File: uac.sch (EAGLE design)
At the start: 206 parts, among them Q6 2N7002CK4SST, Q7 2N7002CK4SST, U2 ADXL345, Y1 RESONATORSMD

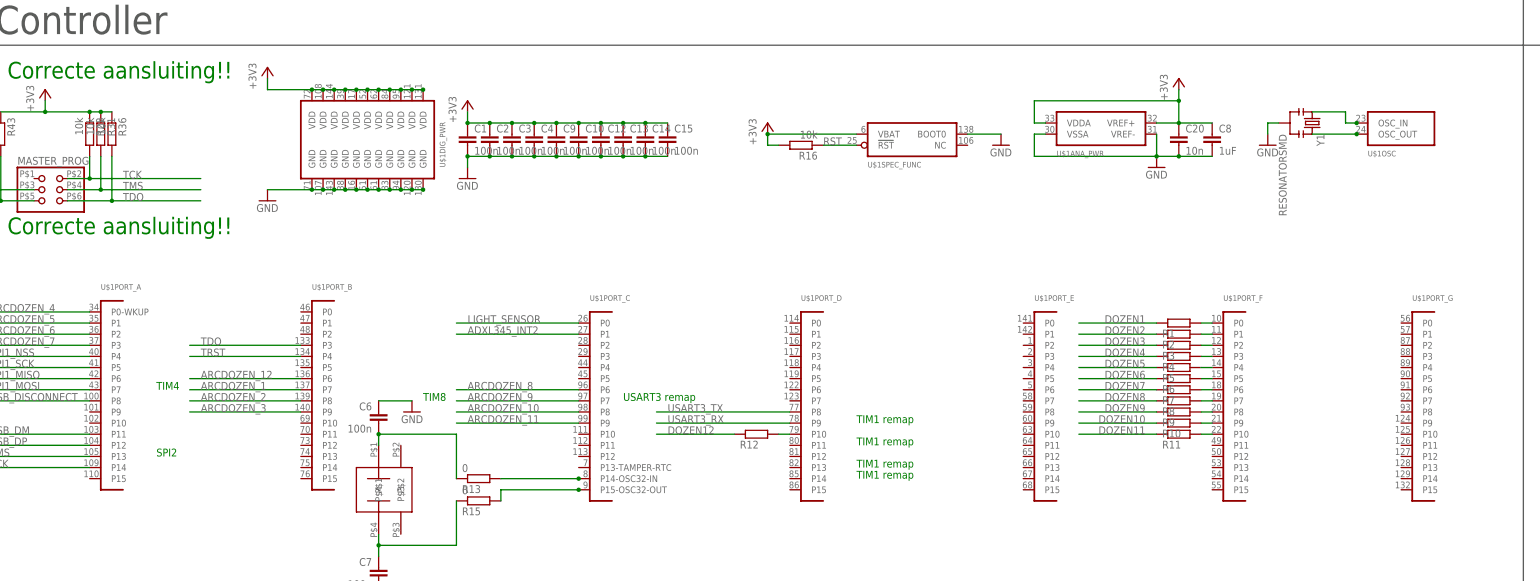
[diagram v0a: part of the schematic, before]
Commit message: Moved to 2 layer
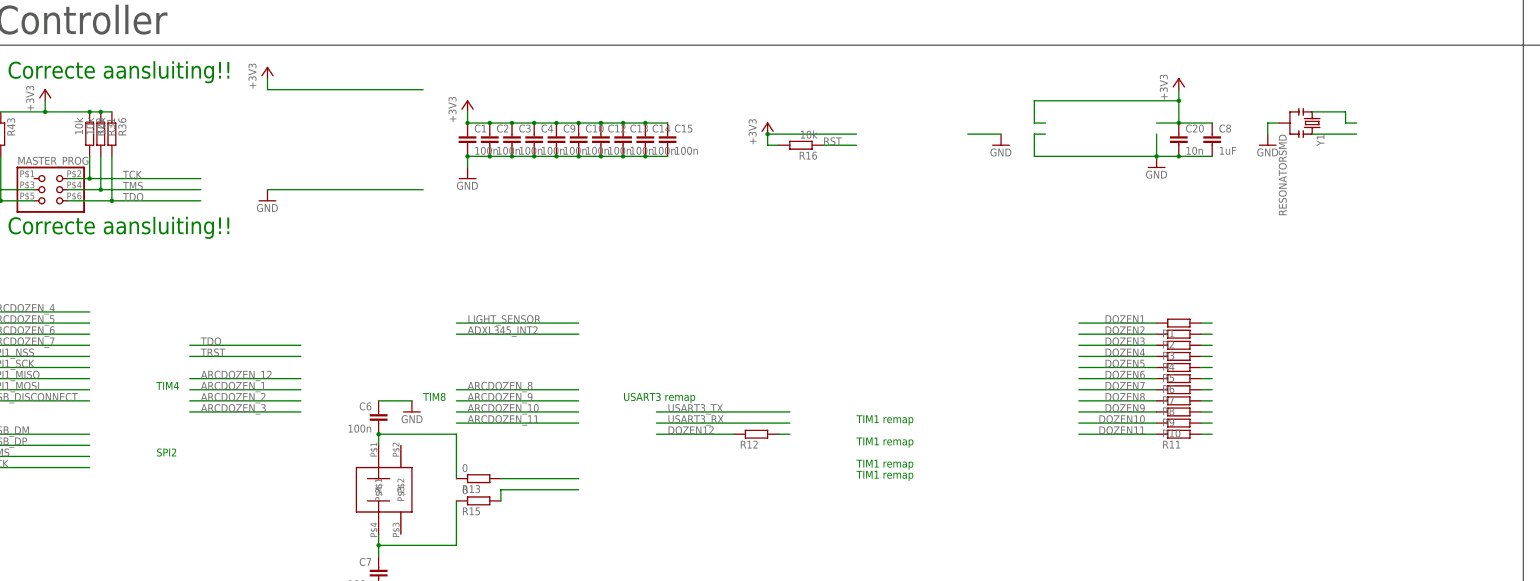
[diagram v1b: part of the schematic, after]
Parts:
- removed U$1: (no value), stm32_lqfp144:STM32F103ZE
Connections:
- net +3V3: no longer U$1ANA_PWR.VDDA, U$1ANA_PWR.VREF+, U$1DIG_PWR.VDD@1, U$1DIG_PWR.VDD@10, U$1DIG_PWR.VDD@11, U$1DIG_PWR.VDD@2, U$1DIG_PWR.VDD@3, U$1DIG_PWR.VDD@4, U$1DIG_PWR.VDD@5, U$1DIG_PWR.VDD@6, U$1DIG_PWR.VDD@7, U$1DIG_PWR.VDD@8, U$1DIG_PWR.VDD@9, U$1SPEC_FUNC.VBAT
- net ADXL345_INT2: no longer U$1PORT_C.P1
- net ARCDOZEN_1: no longer U$1PORT_B.P7
- net ARCDOZEN_10: no longer U$1PORT_C.P8
- net ARCDOZEN_11: no longer U$1PORT_C.P9
- net ARCDOZEN_12: no longer U$1PORT_B.P6
- net ARCDOZEN_2: no longer U$1PORT_B.P8
- net ARCDOZEN_3: no longer U$1PORT_B.P9
- net ARCDOZEN_4: no longer U$1PORT_A.P0-WKUP
- net ARCDOZEN_5: no longer U$1PORT_A.P1
- net ARCDOZEN_6: no longer U$1PORT_A.P2
- net ARCDOZEN_7: no longer U$1PORT_A.P3
- net ARCDOZEN_8: no longer U$1PORT_C.P6
- net ARCDOZEN_9: no longer U$1PORT_C.P7
- net GND: no longer U$1ANA_PWR.VREF-, U$1ANA_PWR.VSSA, U$1DIG_PWR.GND@1, U$1DIG_PWR.GND@10, U$1DIG_PWR.GND@11, U$1DIG_PWR.GND@2, U$1DIG_PWR.GND@3, U$1DIG_PWR.GND@4, U$1DIG_PWR.GND@5, U$1DIG_PWR.GND@6, U$1DIG_PWR.GND@7, U$1DIG_PWR.GND@8, U$1DIG_PWR.GND@9, U$1SPEC_FUNC.BOOT0
- net LIGHT_SENSOR: no longer U$1PORT_C.P0
- net N$1: no longer U$1OSC.OSC_OUT
- net N$10: no longer U$1PORT_F.P3
- net N$11: no longer U$1PORT_F.P4
- net N$12: no longer U$1PORT_F.P5
- net N$13: no longer U$1PORT_F.P6
- net N$14: no longer U$1PORT_F.P7
- net N$15: no longer U$1PORT_F.P8
- net N$16: no longer U$1PORT_F.P9
- net N$17: no longer U$1PORT_F.P10
- net N$2: no longer U$1OSC.OSC_IN
- net N$3: no longer U$1PORT_C.P15-OSC32-OUT
- net N$35: no longer U$1PORT_D.P10
- net N$4: no longer U$1PORT_C.P14-OSC32-IN
- net N$7: no longer U$1PORT_F.P0
- net N$8: no longer U$1PORT_F.P1
- net N$9: no longer U$1PORT_F.P2
- net RST: no longer U$1SPEC_FUNC.!RST
- net SPI1_MISO: no longer U$1PORT_A.P6
- net SPI1_MOSI: no longer U$1PORT_A.P7
- net SPI1_NSS: no longer U$1PORT_A.P4
- net SPI1_SCK: no longer U$1PORT_A.P5
- net TCK: no longer U$1PORT_A.P14
- net TDO: no longer U$1PORT_B.P3
- net TMS: no longer U$1PORT_A.P13
- net TRST: no longer U$1PORT_B.P4
- net USART3_RX: no longer U$1PORT_D.P9
- net USART3_TX: no longer U$1PORT_D.P8
- net USB_DISCONNECT: no longer U$1PORT_A.P8
- net USB_DM: no longer U$1PORT_A.P11
- net USB_DP: no longer U$1PORT_A.P12

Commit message: 64 pin  microcontroller
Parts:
- added U$1: STM32F103CBT6, stm32:STM32F103CBT6
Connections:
- net +3V3: now also U$1.VBAT, U$1.VDD_1, U$1.VDD_2, U$1.VDD_3, U$1.VDD_4, U$1.VDD_A
- net GND: now also U$1.VSS_1, U$1.VSS_2, U$1.VSS_3, U$1.VSS_4, U$1.VSS_A
- net N$3: now also U$1.PC14-OSC32_IN
- net N$4: now also U$1.PC15-OSC32_OUT
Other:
- moved on the sheet: C6, C7, R13, R15
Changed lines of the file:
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@@
 <part name="GND9" library="Custom components" deviceset="GND" device=""/>
 <part name="+3V7" library="supply1" deviceset="+3V3" device=""/>
-<part name="GND10" library="Custom components" deviceset="GND" device=""/>
 <part name="R16" library="Custom components" deviceset="R-EU_" device="R0603" value="10k"/>
 <part name="C9" library="Custom components" deviceset="C-EU" device="C0603" value="100n"/>
@@
 <part name="P+3" library="Custom components" deviceset="+5V" device=""/>
 <part name="JP1" library="SparkFun2012" deviceset="JUMPER-2" device="SMD-NO"/>
+<part name="U$1" library="stm32" deviceset="STM32F103CBT6" device=""/>
 </parts>
 <sheets>
@@
 <instance part="R43" gate="G$1" x="25.4" y="215.9" rot="R270"/>
 <instance part="+3V3" gate="G$1" x="35.56" y="226.06"/>
-<instance part="U$2" gate="G$1" x="114.3" y="137.16" rot="MR270"/>
-<instance part="C6" gate="G$1" x="111.76" y="152.4" rot="MR0"/>
-<instance part="C7" gate="G$1" x="111.76" y="116.84" rot="MR0"/>
-<instance part="GND6" gate="1" x="111.76" y="106.68" rot="MR0"/>
-<instance part="GND7" gate="1" x="119.38" y="152.4" rot="MR0"/>
-<instance part="R13" gate="G$1" x="134.62" y="137.16" rot="MR180"/>
-<instance part="R15" gate="G$1" x="134.62" y="132.08" rot="MR180"/>
+<instance part="U$2" gate="G$1" x="231.14" y="342.9" rot="R270"/>
+<instance part="C6" gate="G$1" x="233.68" y="358.14"/>
+<instance part="C7" gate="G$1" x="233.68" y="322.58"/>
+<instance part="GND6" gate="1" x="233.68" y="312.42"/>
+<instance part="GND7" gate="1" x="226.06" y="358.14"/>
+<instance part="R13" gate="G$1" x="210.82" y="342.9" rot="R180"/>
+<instance part="R15" gate="G$1" x="210.82" y="337.82" rot="R180"/>
 <instance part="+3V4" gate="G$1" x="294.64" y="228.6"/>
 <instance part="C20" gate="G$1" x="294.64" y="215.9"/>
 <instance part="C8" gate="G$1" x="302.26" y="215.9"/>
 <instance part="GND8" gate="1" x="289.56" y="208.28"/>
-<instance part="+3V5" gate="G$1" x="86.36" y="231.14"/>
-<instance part="GND9" gate="1" x="86.36" y="200.66"/>
+<instance part="+3V5" gate="G$1" x="154.94" y="401.32"/>
+<instance part="GND9" gate="1" x="154.94" y="299.72"/>
 <instance part="+3V7" gate="G$1" x="200.66" y="218.44"/>
-<instance part="GND10" gate="1" x="254" y="213.36"/>
 <instance part="R16" gate="G$1" x="208.28" y="213.36" rot="R180"/>
 <instance part="C9" gate="G$1" x="152.4" y="215.9"/>
@@
 <instance part="P+3" gate="1" x="424.18" y="134.62"/>
 <instance part="JP1" gate="A" x="419.1" y="134.62"/>
+<instance part="U$1" gate="G$1" x="149.86" y="363.22"/>
 </instances>
 <busses>
@@
 <pinref part="C7" gate="G$1" pin="2"/>
 <pinref part="GND6" gate="1" pin="GND"/>
-<wire x1="111.76" y1="109.22" x2="111.76" y2="111.76" width="0.1524" layer="91"/>
+<wire x1="233.68" y1="314.96" x2="233.68" y2="317.5" width="0.1524" layer="91"/>
 </segment>
 <segment>
 <pinref part="C6" gate="G$1" pin="1"/>
 <pinref part="GND7" gate="1" pin="GND"/>
-<wire x1="111.76" y1="154.94" x2="119.38" y2="154.94" width="0.1524" layer="91"/>
+<wire x1="233.68" y1="360.68" x2="226.06" y2="360.68" width="0.1524" layer="91"/>
 </segment>
 <segment>
@@
 <pinref part="GND8" gate="1" pin="GND"/>
 <wire x1="294.64" y1="210.82" x2="289.56" y2="210.82" width="0.1524" layer="91"/>
-<wire x1="289.56" y1="210.82" x2="289.56" y2="215.9" width="0.1524" layer="91"/>
-<wire x1="264.16" y1="215.9" x2="261.62" y2="215.9" width="0.1524" layer="91"/>
-<wire x1="261.62" y1="215.9" x2="261.62" y2="210.82" width="0.1524" layer="91"/>
-<wire x1="261.62" y1="210.82" x2="289.56" y2="210.82" width="0.1524" layer="91"/>
-<junction x="289.56" y="210.82"/>
 <junction x="294.64" y="210.82"/>
-</segment>
-<segment>
-<wire x1="121.92" y1="203.2" x2="86.36" y2="203.2" width="0.1524" layer="91"/>
-<pinref part="GND9" gate="1" pin="GND"/>
-</segment>
-<segment>
-<pinref part="GND10" gate="1" pin="GND"/>
-<wire x1="246.38" y1="215.9" x2="254" y2="215.9" width="0.1524" layer="91"/>
 </segment>
 <segment>
@@
 <wire x1="175.26" y1="20.32" x2="177.8" y2="20.32" width="0.1524" layer="91"/>
 </segment>
+<segment>
+<pinref part="GND9" gate="1" pin="GND"/>
+<pinref part="U$1" gate="G$1" pin="VSS_A"/>
+<wire x1="154.94" y1="302.26" x2="154.94" y2="304.8" width="0.1524" layer="91"/>
+<pinref part="U$1" gate="G$1" pin="VSS_1"/>
+<wire x1="154.94" y1="304.8" x2="160.02" y2="304.8" width="0.1524" layer="91"/>
+<pinref part="U$1" gate="G$1" pin="VSS_2"/>
+<wire x1="160.02" y1="304.8" x2="162.56" y2="304.8" width="0.1524" layer="91"/>
+<pinref part="U$1" gate="G$1" pin="VSS_3"/>
+<wire x1="162.56" y1="304.8" x2="165.1" y2="304.8" width="0.1524" layer="91"/>
+<pinref part="U$1" gate="G$1" pin="VSS_4"/>
+<wire x1="165.1" y1="304.8" x2="167.64" y2="304.8" width="0.1524" layer="91"/>
+<junction x="154.94" y="304.8"/>
+<junction x="160.02" y="304.8"/>
+<junction x="162.56" y="304.8"/>
+<junction x="165.1" y="304.8"/>
+<junction x="167.64" y="304.8"/>
+</segment>
 </net>
 <net name="+3V3" class="0">
@@
 </segment>
 <segment>
-<wire x1="289.56" y1="218.44" x2="294.64" y2="218.44" width="0.1524" layer="91"/>
-<wire x1="294.64" y1="218.44" x2="294.64" y2="223.52" width="0.1524" layer="91"/>
-<wire x1="294.64" y1="223.52" x2="261.62" y2="223.52" width="0.1524" layer="91"/>
-<wire x1="261.62" y1="223.52" x2="261.62" y2="218.44" width="0.1524" layer="91"/>
-<wire x1="261.62" y1="218.44" x2="264.16" y2="218.44" width="0.1524" layer="91"/>
+<wire x1="294.64" y1="218.44" x2="294.64" y2="226.06" width="0.1524" layer="91"/>
 <pinref part="+3V4" gate="G$1" pin="+3V3"/>
-<wire x1="294.64" y1="226.06" x2="294.64" y2="223.52" width="0.1524" layer="91"/>
-<junction x="294.64" y="223.52"/>
 <pinref part="C20" gate="G$1" pin="1"/>
 <pinref part="C8" gate="G$1" pin="1"/>
 <wire x1="294.64" y1="218.44" x2="302.26" y2="218.44" width="0.1524" layer="91"/>
 <junction x="294.64" y="218.44"/>
-</segment>
-<segment>
-<wire x1="121.92" y1="226.06" x2="86.36" y2="226.06" width="0.1524" layer="91"/>
-<pinref part="+3V5" gate="G$1" pin="+3V3"/>
-<wire x1="86.36" y1="228.6" x2="86.36" y2="226.06" width="0.1524" layer="91"/>
 </segment>
 <segment>
@@
 <wire x1="177.8" y1="7.62" x2="177.8" y2="10.16" width="0.1524" layer="91"/>
 </segment>
+<segment>
+<pinref part="U$1" gate="G$1" pin="VBAT"/>
+<pinref part="U$1" gate="G$1" pin="VDD_4"/>
+<wire x1="172.72" y1="391.16" x2="167.64" y2="391.16" width="0.1524" layer="91"/>
+<pinref part="U$1" gate="G$1" pin="VDD_3"/>
+<wire x1="167.64" y1="391.16" x2="165.1" y2="391.16" width="0.1524" layer="91"/>
+<pinref part="U$1" gate="G$1" pin="VDD_2"/>
+<wire x1="165.1" y1="391.16" x2="162.56" y2="391.16" width="0.1524" layer="91"/>
+<pinref part="U$1" gate="G$1" pin="VDD_1"/>
+<wire x1="162.56" y1="391.16" x2="160.02" y2="391.16" width="0.1524" layer="91"/>
+<pinref part="U$1" gate="G$1" pin="VDD_A"/>
+<wire x1="160.02" y1="391.16" x2="154.94" y2="391.16" width="0.1524" layer="91"/>
+<pinref part="+3V5" gate="G$1" pin="+3V3"/>
+<wire x1="154.94" y1="391.16" x2="154.94" y2="398.78" width="0.1524" layer="91"/>
+<junction x="154.94" y="391.16"/>
+<junction x="160.02" y="391.16"/>
+<junction x="162.56" y="391.16"/>
+<junction x="165.1" y="391.16"/>
+<junction x="167.64" y="391.16"/>
+<junction x="172.72" y="391.16"/>
+</segment>
 </net>
 <net name="N$1" class="0">
@@
 <segment>
 <pinref part="R15" gate="G$1" pin="2"/>
-<wire x1="139.7" y1="132.08" x2="139.7" y2="134.62" width="0.1524" layer="91"/>
-<wire x1="139.7" y1="134.62" x2="157.48" y2="134.62" width="0.1524" layer="91"/>
+<wire x1="205.74" y1="337.82" x2="205.74" y2="340.36" width="0.1524" layer="91"/>
+<wire x1="205.74" y1="340.36" x2="187.96" y2="340.36" width="0.1524" layer="91"/>
+<pinref part="U$1" gate="G$1" pin="PC14-OSC32_IN"/>
+<junction x="187.96" y="340.36"/>
 </segment>
 </net>
@@
 <segment>
 <pinref part="R13" gate="G$1" pin="2"/>
-<wire x1="157.48" y1="137.16" x2="139.7" y2="137.16" width="0.1524" layer="91"/>
+<wire x1="187.96" y1="342.9" x2="205.74" y2="342.9" width="0.1524" layer="91"/>
+<pinref part="U$1" gate="G$1" pin="PC15-OSC32_OUT"/>
+<junction x="187.96" y="342.9"/>
 </segment>
 </net>
@@
 <segment>
 <pinref part="R13" gate="G$1" pin="1"/>
-<wire x1="129.54" y1="137.16" x2="129.54" y2="147.32" width="0.1524" layer="91"/>
+<wire x1="215.9" y1="342.9" x2="215.9" y2="353.06" width="0.1524" layer="91"/>
 <pinref part="C6" gate="G$1" pin="2"/>
 <pinref part="U$2" gate="G$1" pin="P$1"/>
-<wire x1="111.76" y1="147.32" x2="111.76" y2="144.78" width="0.1524" layer="91"/>
-<wire x1="129.54" y1="147.32" x2="111.76" y2="147.32" width="0.1524" layer="91"/>
-<junction x="111.76" y="147.32"/>
+<wire x1="233.68" y1="353.06" x2="233.68" y2="350.52" width="0.1524" layer="91"/>
+<wire x1="215.9" y1="353.06" x2="233.68" y2="353.06" width="0.1524" layer="91"/>
+<junction x="233.68" y="353.06"/>
 </segment>
 </net>
@@
 <segment>
 <pinref part="R15" gate="G$1" pin="1"/>
-<wire x1="129.54" y1="132.08" x2="129.54" y2="121.92" width="0.1524" layer="91"/>
+<wire x1="215.9" y1="337.82" x2="215.9" y2="327.66" width="0.1524" layer="91"/>
 <pinref part="C7" gate="G$1" pin="1"/>
 <pinref part="U$2" gate="G$1" pin="P$4"/>
-<wire x1="111.76" y1="119.38" x2="111.76" y2="121.92" width="0.1524" layer="91"/>
-<wire x1="111.76" y1="121.92" x2="111.76" y2="124.46" width="0.1524" layer="91"/>
-<wire x1="129.54" y1="121.92" x2="111.76" y2="121.92" width="0.1524" layer="91"/>
-<junction x="111.76" y="121.92"/>
-</segment>
-</net>
+<wire x1="233.68" y1="325.12" x2="233.68" y2="327.66" width="0.1524" layer="91"/>
+<wire x1="233.68" y1="327.66" x2="233.68" y2="330.2" width="0.1524" layer="91"/>
+<wire x1="215.9" y1="327.66" x2="233.68" y2="327.66" width="0.1524" layer="91"/>
+<junction x="233.68" y="327.66"/>
+</segment>
+</net>
